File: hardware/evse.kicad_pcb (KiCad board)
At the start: 2 copper layers, 42.5 x 62.5 mm, 87 parts, among them J101 Boot, J102 Power Setting, P101 CON-SENSOR2, P102 Relay, P104 12V/Motor/GP, P105 CP/PP/PE, U101 XMC1100, U102 PEM1-S12-D12-S, U103 MAX14850, U104 ADS1118I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

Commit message: change to xmc1302
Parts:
- U101: value XMC1100 -> XMC1302
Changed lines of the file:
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@@
       (effects (font (size 0.3 0.3) (thickness 0.075)))
     )
-    (fp_text value XMC1100 (at 0 0.8 90) (layer F.Fab)
+    (fp_text value XMC1302 (at 0 0.8 90) (layer F.Fab)
       (effects (font (size 0.3 0.3) (thickness 0.075)))
     )
@@
   (segment (start 159.75 77.9) (end 159.9 77.75) (width 0.15) (layer F.Cu) (net 28))
   (segment (start 159.9 77.75) (end 160.35 77.75) (width 0.15) (layer F.Cu) (net 28))
-  (segment (start 159.424001 78.275999) (end 159.424001 77.675999) (width 0.15) (layer F.Cu) (net 70))
-  (segment (start 159.275 78.425) (end 159.424001 78.275999) (width 0.15) (layer F.Cu) (net 70))
-  (segment (start 159.324001 78.375999) (end 159.275 78.425) (width 0.15) (layer F.Cu) (net 70))
-  (segment (start 159.424001 77.675999) (end 159.85 77.25) (width 0.15) (layer F.Cu) (net 70))
-  (segment (start 159.85 77.25) (end 160.3 77.25) (width 0.15) (layer F.Cu) (net 70))
   (via (at 166.95 96.8) (size 0.55) (drill 0.25) (layers F.Cu B.Cu) (net 29))
   (segment (start 169.85 95.6) (end 169.85 96.450014) (width 0.2) (layer F.Cu) (net 29))
@@
   (segment (start 145.54958 65.64958) (end 145.54958 62.95042) (width 0.7) (layer F.Cu) (net 69))
   (segment (start 145.54958 62.95042) (end 145.55 62.95) (width 0.7) (layer F.Cu) (net 69))
+  (segment (start 159.424001 78.275999) (end 159.424001 77.675999) (width 0.15) (layer F.Cu) (net 70))
+  (segment (start 159.275 78.425) (end 159.424001 78.275999) (width 0.15) (layer F.Cu) (net 70))
+  (segment (start 159.324001 78.375999) (end 159.275 78.425) (width 0.15) (layer F.Cu) (net 70))
+  (segment (start 159.424001 77.675999) (end 159.85 77.25) (width 0.15) (layer F.Cu) (net 70))
+  (segment (start 159.85 77.25) (end 160.3 77.25) (width 0.15) (layer F.Cu) (net 70))
   (segment (start 159.175 78.425) (end 159.275 78.425) (width 0.15) (layer F.Cu) (net 70))
   (segment (start 157.79888 84.39888) (end 157.625519 84.225519) (width 0.15) (layer F.Cu) (net 70))

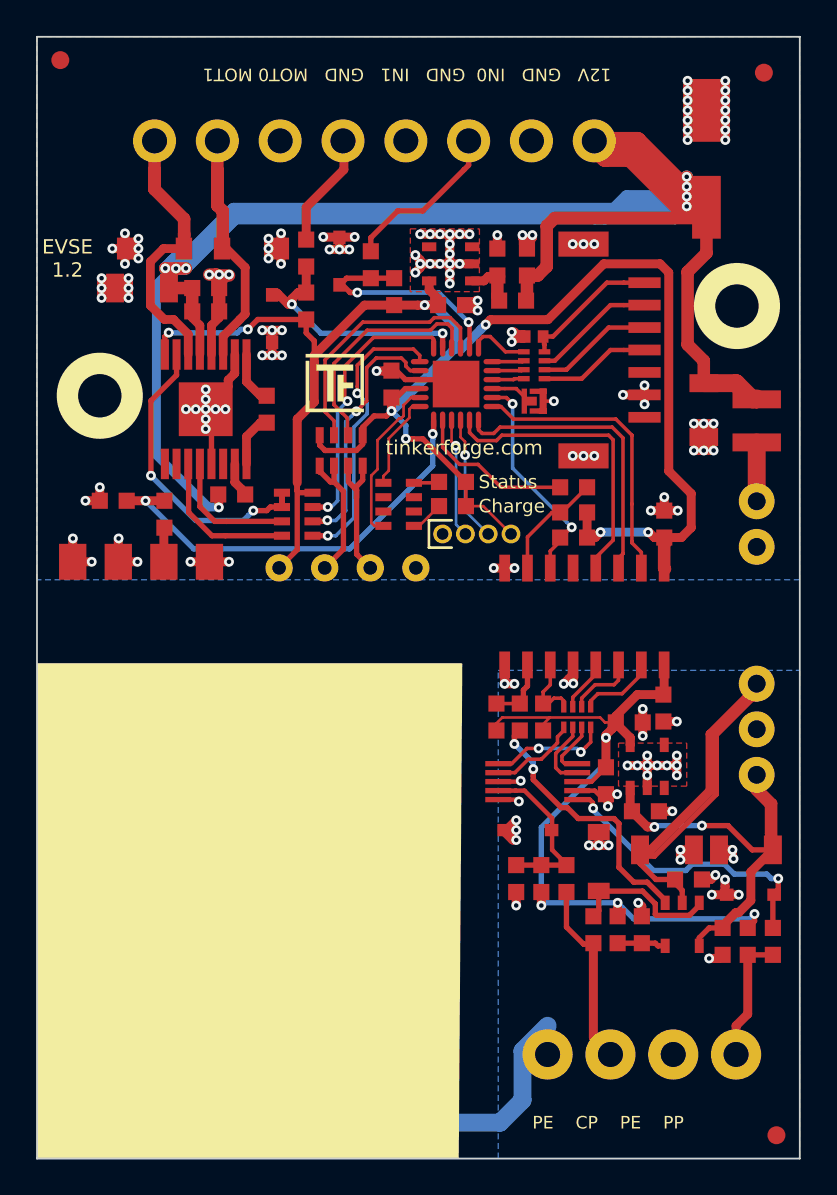
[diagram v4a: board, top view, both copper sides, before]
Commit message: add version 1.3
 * add external output for led control
 * remove internal charge led
 * add cutout
 * change pin mappings
 * change pin silkscreen text
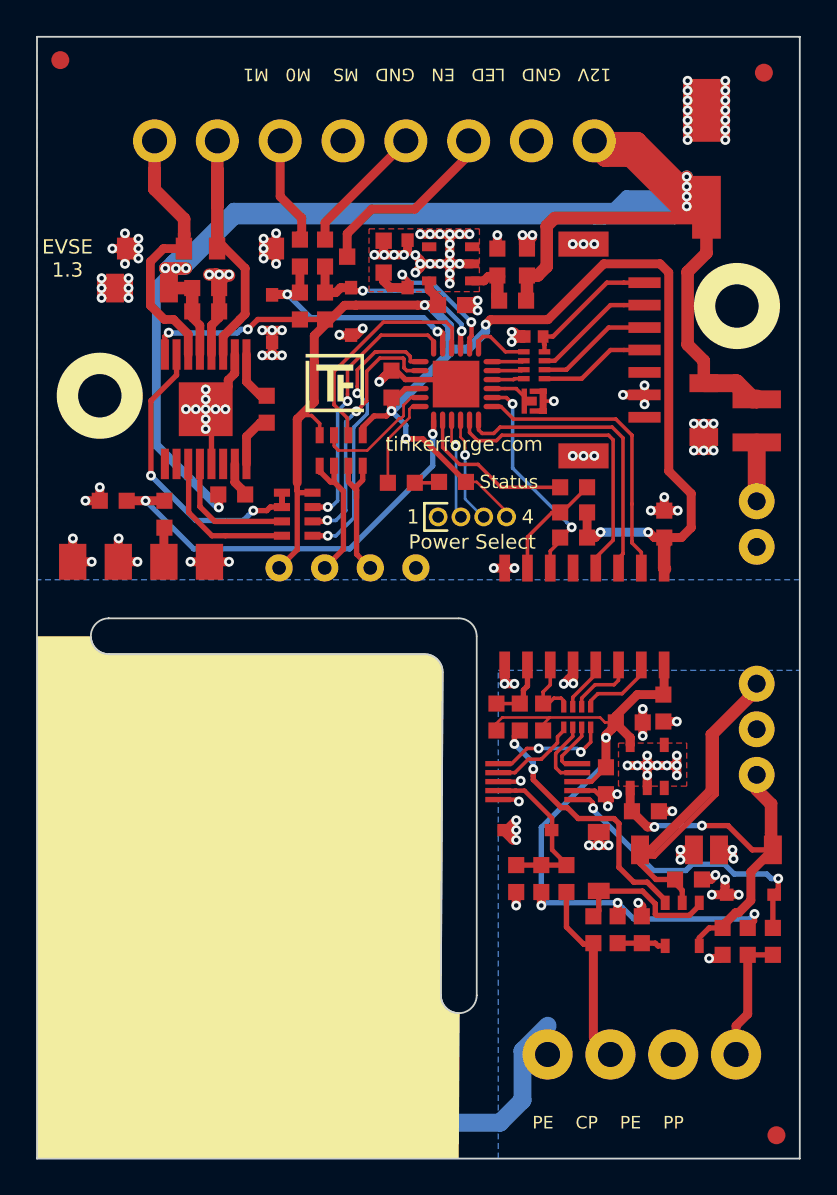
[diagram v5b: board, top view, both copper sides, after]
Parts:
- removed D102: green, kicad-libraries:D0603F
- removed RP102: 1k, kicad-libraries:4X0603
- added D101: ‎PESD3V3L1BA, kicad-libraries:SOD-323, F.Cu at (159.7, 69.8)
- added Q101: 2N7002P, kicad-libraries:SOT23GDS, F.Cu at (157.3, 69.4)
- added R124: 1k, kicad-libraries:R0603F, F.Cu at (159.3, 82.0)
- moved G*** 12.0 mm to (160.2, 78.5)
- moved VAL 12.0 mm to (170.2, 78.5)
- moved VAL 12.0 mm to (150.2, 78.5)
- moved R121 3.93 mm to (155.1, 72.2)
- moved D110 2.87 mm to (156.5, 72.5), turned to 270 degrees
- moved R120 2.63 mm to (155.1, 69.2)
- moved J102 0.98 mm to (161.3, 83.9)
- moved R117 0.35 mm to (153.7, 69.2)
- moved R119 0.35 mm to (153.7, 72.2)
- moved D108 0.27 mm to (150.7, 69.0)
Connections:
- P104 pad 4: GND -> Net-(P104-Pad4)
- P104 pad 5: Net-(P104-Pad5) -> GND
- P104 pad 6: GND -> Net-(P104-Pad6)
- R117 pad 2: Net-(P104-Pad5) -> Net-(P104-Pad6)
- R120 pad 2: Net-(P104-Pad3) -> Net-(P104-Pad4)
- U101 pad 11: Net-(RP102-Pad1) -> AC1
- U101 pad 2: INPUT-GP -> OUTPUT-GP
- U101 pad 3: AC1 -> INPUT-GP
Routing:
- net Net-(RP102-Pad1): track 9.22 -> 0.00 mm
- net OUTPUT-GP: track 0.00 -> 9.17 mm, vias 0 -> 2
- net Net-(P104-Pad4): track 0.00 -> 7.36 mm
- net Net-(P104-Pad5): track 6.39 -> 0.00 mm
- net AC1: track 14.3 -> 8.12 mm
- net Net-(P104-Pad6): track 0.00 -> 6.10 mm
- net 3V3: track 102.1 -> 100.0 mm
- net Net-(D102-Pad2): track 1.91 -> 0.00 mm
- net Net-(P104-Pad3): track 9.23 -> 10.7 mm
- net GND: track 93.2 -> 94.5 mm, vias 108 -> 109
- net INPUT-GP: track 12.6 -> 11.3 mm
- net Net-(J102-Pad2): track 6.64 -> 5.58 mm
- net Net-(J102-Pad3): track 6.96 -> 5.96 mm
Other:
- outline, holes or cut-outs redrawn
- board text added: "1"
- board text added: "12V GND LED EN GND MS M0 M1"
- board text added: "4"
- board text added: "EVSE 1.3"
- board text added: "Power Select"
- board text removed: "12V GND IN0 GND IN1 GND MOT0 MOT1"
- board text removed: "Charge"
- board text removed: "EVSE 1.2"

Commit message: start version 1.4, change configuration header
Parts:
- J102: value Power Setting -> Config; footprint kicad-libraries:Pin_Header_Straight_1x04_127 -> kicad-libraries:Pin_Header_Straight_2x03_127
- moved J102 2.10 mm to (163.4, 84.3)
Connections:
- J102 pad 1: GND -> 3V3
- J102 pad 2: Net-(J102-Pad2) -> 3V3
- J102 pad 4: 3V3 -> Net-(J102-Pad4)
- U101 pad 15: Net-(J102-Pad2) -> Net-(J102-Pad4)
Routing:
- net Net-(J102-Pad4): track 0.00 -> 5.96 mm, vias 0 -> 1
- net Net-(J102-Pad2): track 5.58 -> 0.00 mm, vias 1 -> 0
- net Net-(J102-Pad3): track 5.96 -> 11.3 mm
- net GND: track 94.5 -> 97.8 mm
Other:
- board text added: "CONF"
- board text added: "EVSE 1.4"
- board text added: "LSS"
- board text added: "MPS"
- board text removed: "1"
- board text removed: "4"
- board text removed: "EVSE 1.3"
- board text removed: "Power Select"

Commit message: ordered version
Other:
- board text added: "PWR"
- board text removed: "CONF"
- board text removed: "LSS"
- board text removed: "MPS"
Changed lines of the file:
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@@
   (general
     (thickness 1.6)
-    (drawings 25)
+    (drawings 23)
     (tracks 1160)
     (zones 0)
@@
   )
   (setup
-    (last_trace_width 0.25)
+    (last_trace_width 0.15)
     (user_trace_width 0.15)
     (user_trace_width 0.2)
@@
     (visible_elements FFFFFFFF)
     (pcbplotparams
-      (layerselection 0x00080_7ffffffe)
+      (layerselection 0x00044_fffffffe)
       (usegerberextensions true)
       (usegerberattributes false)
@@
     )
   )
-  (gr_text MPS (at 165.3 83.7) (layer F.SilkS)
-    (effects (font (size 0.7 0.7) (thickness 0.15)) (justify left))
+  (gr_text "High\nVoltage\nArea" (at 151.3 100.35) (layer F.Mask)
+    (effects (font (size 1 1) (thickness 0.15)))
   )
   (gr_line (start 162.5 89.55) (end 143 89.55) (layer Edge.Cuts) (width 0.09906))
@@
   (gr_arc (start 162.5 110.55) (end 161.5 110.55) (angle -180) (layer Edge.Cuts) (width 0.09906))
   (gr_arc (start 143 90.55) (end 143 89.55) (angle -180) (layer Edge.Cuts) (width 0.09906))
-  (gr_text LSS (at 165.3 85) (layer F.SilkS)
-    (effects (font (size 0.7 0.7) (thickness 0.15)) (justify left))
-  )
-  (gr_text CONF (at 160.65 84.35 90) (layer F.SilkS)
+  (gr_text PWR (at 160.65 84.35 90) (layer F.SilkS)
     (effects (font (size 0.7 0.7) (thickness 0.15)))
   )
@@
     (effects (font (size 0.8 0.8) (thickness 0.15)))
   )
-  (gr_text "High\nVoltage\nArea" (at 151.3 100.35) (layer F.Mask)
-    (effects (font (size 1 1) (thickness 0.15)))
-  )
   (gr_text "REL0  REL1  PE    PE   AC0   AC1" (at 141.5 117.65) (layer F.Mask)
     (effects (font (size 0.7 0.7) (thickness 0.15)) (justify left))
@@
   (segment (start 166.163522 99.150998) (end 167.7 100.687476) (width 0.25) (layer F.Cu) (net 78))
   (segment (start 165.675 99.15) (end 165.675998 99.150998) (width 0.25) (layer F.Cu) (net 78))
-  (segment (start 162.1 79.711989) (end 162.325095 79.937084) (width 0.15) (layer F.Cu) (net 84))
-  (segment (start 162.1 78.525) (end 162.1 79.711989) (width 0.15) (layer F.Cu) (net 84))
-  (via (at 162.325095 79.937084) (size 0.55) (drill 0.25) (layers F.Cu B.Cu) (net 84))
-  (segment (start 162.35 79.961989) (end 162.325095 79.937084) (width 0.15) (layer B.Cu) (net 84))
   (segment (start 163.4 84.985) (end 164.315 85.9) (width 0.25) (layer B.Cu) (net 79))
   (segment (start 164.315 85.9) (end 165.15 85.9) (width 0.25) (layer B.Cu) (net 79))
@@
   (segment (start 162.89901 79.760102) (end 162.89901 80.45) (width 0.15) (layer F.Cu) (net 79))
   (via (at 162.89901 80.45) (size 0.55) (drill 0.25) (layers F.Cu B.Cu) (net 79))
-  (segment (start 163.4 83.55) (end 163.4 83.75) (width 0.25) (layer B.Cu) (net 84))
   (segment (start 155.05 67.5) (end 159.55 63) (width 0.5) (layer F.Cu) (net 80))
   (segment (start 155.05 68.45) (end 155.05 67.5) (width 0.5) (layer F.Cu) (net 80))
@@
   (segment (start 158.55 82) (end 158.55 79.575) (width 0.15) (layer F.Cu) (net 83))
   (segment (start 158.55 79.575) (end 158.6 79.525) (width 0.15) (layer F.Cu) (net 83))
+  (segment (start 162.1 79.711989) (end 162.325095 79.937084) (width 0.15) (layer F.Cu) (net 84))
+  (segment (start 162.1 78.525) (end 162.1 79.711989) (width 0.15) (layer F.Cu) (net 84))
+  (via (at 162.325095 79.937084) (size 0.55) (drill 0.25) (layers F.Cu B.Cu) (net 84))
+  (segment (start 162.35 79.961989) (end 162.325095 79.937084) (width 0.15) (layer B.Cu) (net 84))
+  (segment (start 163.4 83.55) (end 163.4 83.75) (width 0.25) (layer B.Cu) (net 84))
   (segment (start 162.35 82.15) (end 162.35 80) (width 0.25) (layer B.Cu) (net 84))
   (segment (start 163.4 83.715) (end 163.4 83.2) (width 0.25) (layer B.Cu) (net 84))
@@
     )
   )
-  (zone (net 0) (net_name "") (layer F.Mask) (hatch edge 0.508)
+  (zone (net 0) (net_name "") (layer F.SilkS) (hatch edge 0.508)
     (connect_pads yes (clearance 0))
     (min_thickness 0.1)
@@
     (polygon
       (pts
-        (xy 147.2 99.75) (xy 148.25 99.75) (xy 145.85 102.65) (xy 145.5 102.65) (xy 146.65 100.35)
-        (xy 146.6 100.35) (xy 145.55 100.35) (xy 146.5 98) (xy 148.15 98)
+        (xy 162.7 90.55) (xy 162.5 119.65) (xy 139 119.65) (xy 139 90.55)
       )
     )
   )
-  (zone (net 0) (net_name "") (layer F.SilkS) (hatch edge 0.508)
+  (zone (net 0) (net_name "") (layer F.Mask) (hatch edge 0.508)
     (connect_pads yes (clearance 0))
     (min_thickness 0.1)
@@
     (polygon
       (pts
-        (xy 162.7 90.55) (xy 162.5 119.65) (xy 139 119.65) (xy 139 90.55)
+        (xy 147.2 99.75) (xy 148.25 99.75) (xy 145.85 102.65) (xy 145.5 102.65) (xy 146.65 100.35)
+        (xy 146.6 100.35) (xy 145.55 100.35) (xy 146.5 98) (xy 148.15 98)
       )
     )

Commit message: mark diode as DNP
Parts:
- D106: value ‎PESD5V0L1BA -> DNP
